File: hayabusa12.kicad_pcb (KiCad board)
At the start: 2 copper layers, 118.3 x 57.1 mm, 32 parts, among them J1 USB_C_Receptacle_USB2.0, SW1 SW_Push, SW10 MX_SW_HS, SW11 MX_SW_HS, SW12 MX_SW_HS, SW13 MX_SW_HS, SW2 MX_SW_HS, SW3 MX_SW_HS, SW4 MX_SW_HS, SW5 MX_SW_HS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

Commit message: routing
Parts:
- moved SW11 57.2 mm to (247.7, 61.9)
- moved SW12 57.2 mm to (247.7, 81.0)
- moved SW13 57.2 mm to (247.7, 100.0)
- moved SW2 57.2 mm to (190.5, 61.9)
- moved SW3 57.2 mm to (190.5, 81.0)
- moved SW4 57.2 mm to (190.5, 100.0)
- moved SW10 19.0 mm to (228.6, 100.0)
- moved SW5 19.0 mm to (209.6, 61.9)
- moved SW6 19.0 mm to (209.6, 81.0)
- moved SW7 19.0 mm to (209.6, 100.0)
- moved SW8 19.0 mm to (228.6, 61.9)
- moved SW9 19.0 mm to (228.6, 81.0)
- moved SW1 2.51 mm to (151.6, 88.9)
- moved C7 1.46 mm to (158.9, 84.9)
- moved C6 1.41 mm to (158.5, 79.6), turned to -90 degrees
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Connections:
- U1 pad 26: unconnected-(U1-Pad26) -> ROW0
- U1 pad 27: ROW0 -> ROW1
- U1 pad 28: COL1 -> COL3
- U1 pad 29: COL0 -> COL2
- U1 pad 30: ROW1 -> COL1
- U1 pad 31: unconnected-(U1-Pad31) -> COL0
- U1 pad 32: unconnected-(U1-Pad32) -> ROW2
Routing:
- net +5V: track 16.9 -> 142.9 mm, vias 0 -> 5
- net COL3: track 0.00 -> 119.6 mm
- net GND: track 84.8 -> 192.6 mm, vias 0 -> 3
- net COL2: track 0.00 -> 100.3 mm
- net COL1: track 0.00 -> 80.9 mm
- net ROW0: track 0.00 -> 72.3 mm
- net SDA: track 0.00 -> 70.2 mm, vias 0 -> 2
- net ROW2: track 0.00 -> 67.3 mm
- net COL0: track 0.00 -> 62.5 mm
- net ROW1: track 0.00 -> 55.3 mm
- net SCL: track 0.00 -> 41.7 mm, vias 0 -> 2
- net Net-(R3-Pad2): track 11.2 -> 27.0 mm, vias 0 -> 2
- net Net-(C6-Pad1): track 0.00 -> 5.52 mm

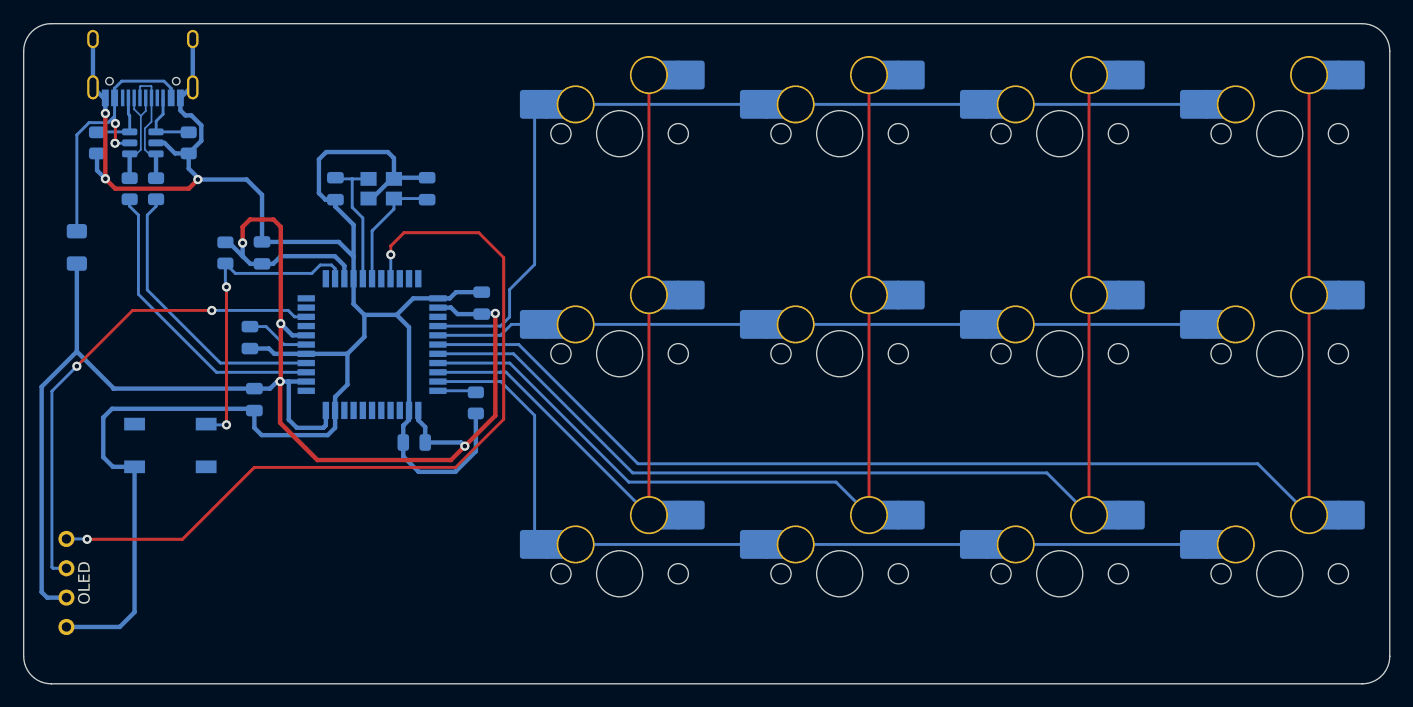
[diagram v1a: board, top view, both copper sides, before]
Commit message: added diodes bc i forgor
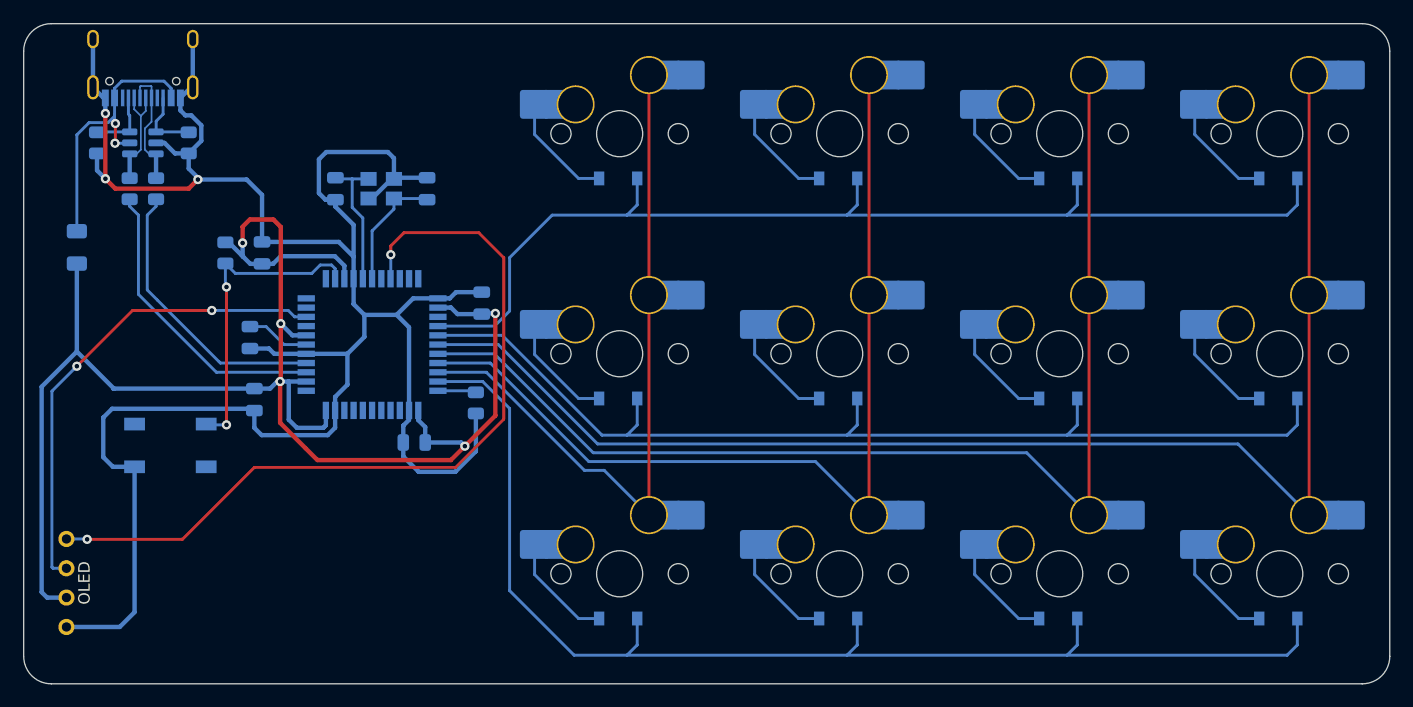
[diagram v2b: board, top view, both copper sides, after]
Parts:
- added D1: D_Small, Diode_SMD:D_SOD-123, B.Cu at (190.4, 65.8)
- added D10: D_Small, Diode_SMD:D_SOD-123, B.Cu at (247.5, 65.8)
- added D11: D_Small, Diode_SMD:D_SOD-123, B.Cu at (247.5, 84.8)
- added D12: D_Small, Diode_SMD:D_SOD-123, B.Cu at (247.5, 103.9)
- added D2: D_Small, Diode_SMD:D_SOD-123, B.Cu at (190.4, 84.8)
- added D3: D_Small, Diode_SMD:D_SOD-123, B.Cu at (190.4, 103.9)
- added D4: D_Small, Diode_SMD:D_SOD-123, B.Cu at (209.4, 65.8)
- added D5: D_Small, Diode_SMD:D_SOD-123, B.Cu at (209.4, 84.8)
- added D6: D_Small, Diode_SMD:D_SOD-123, B.Cu at (209.4, 103.9)
- added D7: D_Small, Diode_SMD:D_SOD-123, B.Cu at (228.5, 103.9)
- added D8: D_Small, Diode_SMD:D_SOD-123, B.Cu at (228.5, 65.8)
- added D9: D_Small, Diode_SMD:D_SOD-123, B.Cu at (228.5, 84.8)
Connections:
- SW10 pad 1: ROW2 -> Net-(SW10-Pad1)
- SW11 pad 1: ROW0 -> Net-(D10-Pad2)
- SW12 pad 1: ROW1 -> Net-(D11-Pad2)
- SW13 pad 1: ROW2 -> Net-(D12-Pad2)
- SW2 pad 1: ROW0 -> Net-(D1-Pad2)
- SW3 pad 1: ROW1 -> Net-(D2-Pad2)
- SW4 pad 1: ROW2 -> Net-(D3-Pad2)
- SW5 pad 1: ROW0 -> Net-(D4-Pad2)
- SW6 pad 1: ROW1 -> Net-(D5-Pad2)
- SW7 pad 1: ROW2 -> Net-(SW7-Pad1)
- SW8 pad 1: ROW0 -> Net-(D8-Pad2)
- SW9 pad 1: ROW1 -> Net-(D9-Pad2)
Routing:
- net ROW2: track 67.3 -> 106.7 mm
- net ROW1: track 55.3 -> 91.3 mm
- net ROW0: track 72.3 -> 94.4 mm
- net Net-(D2-Pad2): track 0.00 -> 9.78 mm
- net Net-(D12-Pad2): track 0.00 -> 9.78 mm
- net Net-(D11-Pad2): track 0.00 -> 9.78 mm
- net Net-(D10-Pad2): track 0.00 -> 9.78 mm
- net Net-(SW7-Pad1): track 0.00 -> 9.78 mm
- net Net-(SW10-Pad1): track 0.00 -> 9.78 mm
- net Net-(D9-Pad2): track 0.00 -> 9.78 mm
- net Net-(D8-Pad2): track 0.00 -> 9.78 mm
- net Net-(D5-Pad2): track 0.00 -> 9.78 mm
- net Net-(D4-Pad2): track 0.00 -> 9.78 mm
- net Net-(D3-Pad2): track 0.00 -> 9.78 mm
- net Net-(D1-Pad2): track 0.00 -> 9.78 mm

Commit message: cleaned up submodules
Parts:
- SW1: footprint random-keyboard-parts:SKQG-1155865 -> marbastlib-various:SW_SPST_SKQG_WithStem
- moved J1 0.42 mm to (149.2, 55.2)
- moved R1 0.41 mm to (148.1, 67.1)
- moved R2 0.41 mm to (150.4, 67.1)
- moved R5 0.41 mm to (153.2, 63.1)
- moved R6 0.41 mm to (145.3, 63.1)
- moved U2 0.41 mm to (149.2, 63.1)
- turned SW1 to 0 degrees
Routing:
- net Net-(R3-Pad2): track 27.0 -> 33.2 mm
- net GND: track 192.6 -> 198.5 mm

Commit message: made minor changes to routing
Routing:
- net GND: track 198.5 -> 198.6 mm, vias 3 -> 2
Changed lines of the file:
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@@
   (segment (start 143.51 73.155) (end 143.51 80.772) (width 0.381) (layer "B.Cu") (net 1))
   (segment (start 145.981786 60.572286) (end 145.981786 66.225786) (width 0.381) (layer "F.Cu") (net 2))
-  (segment (start 146.84375 67.08775) (end 153.19375 67.08775) (width 0.381) (layer "F.Cu") (net 2))
-  (segment (start 145.981786 66.225786) (end 146.84375 67.08775) (width 0.381) (layer "F.Cu") (net 2))
-  (segment (start 153.19375 67.08775) (end 153.9875 66.294) (width 0.381) (layer "F.Cu") (net 2))
   (via (at 145.981786 60.572286) (size 0.8) (drill 0.4) (layers "F.Cu" "B.Cu") (net 2))
   (via (at 145.981786 66.225786) (size 0.8) (drill 0.4) (layers "F.Cu" "B.Cu") (net 2))
-  (via (at 153.9875 66.294) (size 0.8) (drill 0.4) (layers "F.Cu" "B.Cu") (net 2))
   (segment (start 173.101 91.186) (end 171.77 89.855) (width 0.381) (layer "B.Cu") (net 2))
   (segment (start 146.558 85.725) (end 158.72075 85.725) (width 0.381) (layer "B.Cu") (net 2))
@@
   (segment (start 172.26875 85.86875) (end 172.26875 78.66975) (width 0.381) (layer "B.Cu") (net 2))
   (segment (start 166.93525 83.63575) (end 166.93525 80.96875) (width 0.381) (layer "B.Cu") (net 2))
+  (segment (start 158.21025 66.294) (end 154.14375 66.294) (width 0.381) (layer "B.Cu") (net 2))
   (segment (start 165.89375 67.625) (end 165.034 67.625) (width 0.381) (layer "B.Cu") (net 2))
   (segment (start 165.86875 84.70225) (end 166.93525 83.63575) (width 0.381) (layer "B.Cu") (net 2))
   (segment (start 165.89375 67.625) (end 165.89375 68.23075) (width 0.381) (layer "B.Cu") (net 2))
   (segment (start 159.54375 71.28125) (end 166.18875 71.28125) (width 0.381) (layer "B.Cu") (net 2))
+  (segment (start 154.14375 66.294) (end 153.3405 67.09725) (width 0.381) (layer "B.Cu") (net 2))
   (segment (start 172.26875 87.31925) (end 172.26875 85.86875) (width 0.381) (layer "B.Cu") (net 2))
   (segment (start 174.76875 76.16875) (end 175.79925 76.16875) (width 0.381) (layer "B.Cu") (net 2))
@@
   (segment (start 148.50625 90.75) (end 146.63 90.75) (width 0.381) (layer "B.Cu") (net 2))
   (segment (start 165.227 88.011) (end 159.512 88.011) (width 0.381) (layer "B.Cu") (net 2))
+  (segment (start 146.85325 67.09725) (end 145.981786 66.225786) (width 0.381) (layer "B.Cu") (net 2))
   (segment (start 165.86875 85.86875) (end 165.86875 87.36925) (width 0.381) (layer "B.Cu") (net 2))
   (segment (start 145.975 59.238) (end 145.82 59.238) (width 0.381) (layer "B.Cu") (net 2))
@@
   (segment (start 175.79925 76.16875) (end 176.337 75.631) (width 0.381) (layer "B.Cu") (net 2))
   (segment (start 165.86875 85.86875) (end 165.86875 84.70225) (width 0.381) (layer "B.Cu") (net 2))
+  (segment (start 154.14375 66.294) (end 153.19375 65.344) (width 0.381) (layer "B.Cu") (net 2))
   (segment (start 170.434 63.5) (end 170.9625 64.0285) (width 0.381) (layer "B.Cu") (net 2))
   (segment (start 171.77 87.818) (end 172.26875 87.31925) (width 0.381) (layer "B.Cu") (net 2))
@@
   (segment (start 150.3625 63.119) (end 151.09825 63.119) (width 0.381) (layer "B.Cu") (net 2))
   (segment (start 154.70625 90.75) (end 148.50625 90.75) (width 0.381) (layer "B.Cu") (net 2))
-  (segment (start 153.9875 66.294) (end 158.21025 66.294) (width 0.381) (layer "B.Cu") (net 2))
   (segment (start 173.83125 65.725) (end 171.0625 65.725) (width 0.381) (layer "B.Cu") (net 2))
   (segment (start 145.981786 60.572286) (end 145.981786 59.155214) (width 0.381) (layer "B.Cu") (net 2))
@@
   (segment (start 152.908 60.73775) (end 153.416 60.73775) (width 0.381) (layer "B.Cu") (net 2))
   (segment (start 153.416 60.73775) (end 154.28425 61.606) (width 0.381) (layer "B.Cu") (net 2))
-  (segment (start 153.9875 66.294) (end 153.9875 66.13775) (width 0.381) (layer "B.Cu") (net 2))
   (segment (start 171.77 88.646) (end 171.77 87.818) (width 0.381) (layer "B.Cu") (net 2))
   (segment (start 158.72075 85.725) (end 158.877 85.88125) (width 0.381) (layer "B.Cu") (net 2))
-  (segment (start 153.9875 66.13775) (end 153.19375 65.344) (width 0.381) (layer "B.Cu") (net 2))
   (segment (start 153.545 58.323) (end 153.545 54.143) (width 0.381) (layer "B.Cu") (net 2))
   (segment (start 176.337 75.631) (end 178.562 75.631) (width 0.381) (layer "B.Cu") (net 2))
@@
   (segment (start 167.46875 72.56125) (end 167.46875 74.46875) (width 0.381) (layer "B.Cu") (net 2))
   (segment (start 153.19375 64.0315) (end 153.19375 65.344) (width 0.381) (layer "B.Cu") (net 2))
+  (segment (start 153.3405 67.09725) (end 146.85325 67.09725) (width 0.381) (layer "B.Cu") (net 2))
   (segment (start 153.19375 64.0315) (end 154.28425 62.941) (width 0.381) (layer "B.Cu") (net 2))
   (segment (start 154.28425 61.606) (end 154.28425 62.941) (width 0.381) (layer "B.Cu") (net 2))
